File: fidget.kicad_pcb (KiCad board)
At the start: 2 copper layers, 80.5 x 73.5 mm, 88 parts, among them J1 KEYSTONE 120, J2 KEYSTONE 120, Q1 PEMZ7, U1 MCP73831-2ACI/MC, U2 ESP8285, U3 TLV70033DSE, U4 LIS2DE, U5 TPS60150, U6 TPS60150, U7 TPS60150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

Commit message: PCB design at 4am.. probably a bad idea
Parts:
- removed the C12 at (102.8, 128.8)
- removed the C13 at (104.8, 119.8)
- removed the C14 at (108.8, 126.0)
- removed TP3: RST, Measurement_Points:Measurement_Point_Round-SMD-Pad_Small
- removed the U5 at (113.2, 64.3)
- added C18: 2.2u, Capacitors_SMD:C_0603, F.Cu at (84.7, 71.8)
- added C19: 1u, Capacitors_SMD:C_0603, F.Cu at (85.6, 74.9)
- added C20: 2.2u, Capacitors_SMD:C_0603, F.Cu at (81.1, 72.3)
- added C23: 100n, Capacitors_SMD:C_0402, F.Cu at (86.8, 64.5)
- added U7: TPS60150, Housings_DFN_QFN:DFN-6-1EP_2x2mm_Pitch0.65mm, F.Cu at (83.4, 73.6)
- moved C17 72.2 mm to (107.5, 52.5), turned to 300 degrees
- moved U4 72.2 mm to (110.0, 102.5)
- moved U6 69.5 mm to (105.2, 53.8), turned to 210 degrees
- moved C16 69.3 mm to (103.0, 55.1), turned to 120 degrees
- moved C15 68.8 mm to (106.1, 55.8), turned to 210 degrees
- moved C10 60.8 mm to (100.0, 89.5)
- moved R9 55.4 mm to (112.7, 76.8), turned to 120 degrees
- moved R13 50.5 mm to (94.4, 85.6), turned to 180 degrees
- moved R8 50.4 mm to (111.5, 77.5), turned to 120 degrees
- moved R4 47.0 mm to (94.4, 86.8)
- moved C13 45.8 mm to (111.4, 80.0)
- moved U5 44.8 mm to (111.4, 82.6), turned to 90 degrees
- moved Q1 43.1 mm to (97.2, 86.2), turned to 180 degrees
- moved C12 42.9 mm to (109.2, 82.4), turned to 90 degrees
- moved C14 40.8 mm to (111.4, 85.2), turned to 180 degrees
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- renumbered C18 to C12, C19 to C13, C20 to C14, U7 to U5
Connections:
- C14 pad 1: +5P -> +5C
- U5 pad 3: +5P -> +5C
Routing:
- net +3V3: track 0.00 -> 55.1 mm, vias 0 -> 3
- net /IDX: track 0.00 -> 38.7 mm, vias 0 -> 2
- net +BATT: track 0.00 -> 37.1 mm
- net GND: track 0.00 -> 19.8 mm, vias 0 -> 52
- net +5C: track 0.00 -> 14.9 mm, vias 0 -> 2
- net +5F: track 0.00 -> 12.4 mm, vias 0 -> 2
- net /SCK: track 0.00 -> 9.42 mm, vias 0 -> 2
- net /LCK: track 0.00 -> 7.59 mm
- net /~CS~: track 0.00 -> 7.17 mm, vias 0 -> 2
- net Net-(D21-Pad2): track 0.00 -> 6.90 mm
- net Net-(D10-Pad2): track 0.00 -> 6.90 mm
- net /MOSI: track 0.00 -> 6.89 mm
- net /MISO: track 0.00 -> 6.86 mm, vias 0 -> 2
- net Net-(D21-Pad3): track 0.00 -> 5.97 mm
- net Net-(D10-Pad3): track 0.00 -> 5.97 mm
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- added copper zone on F.Cu, net +5C
- added copper zone on F.Cu, net +5F
- added copper zone on F.Cu, net +5P
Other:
- net class Default: clearance 0.2 -> 0.16
- rule pad_to_mask_clearance: 0.2 -> 0.1
- rule trace_clearance: 0.2 -> 0.16
- rule trace_min: 0.2 -> 0.16

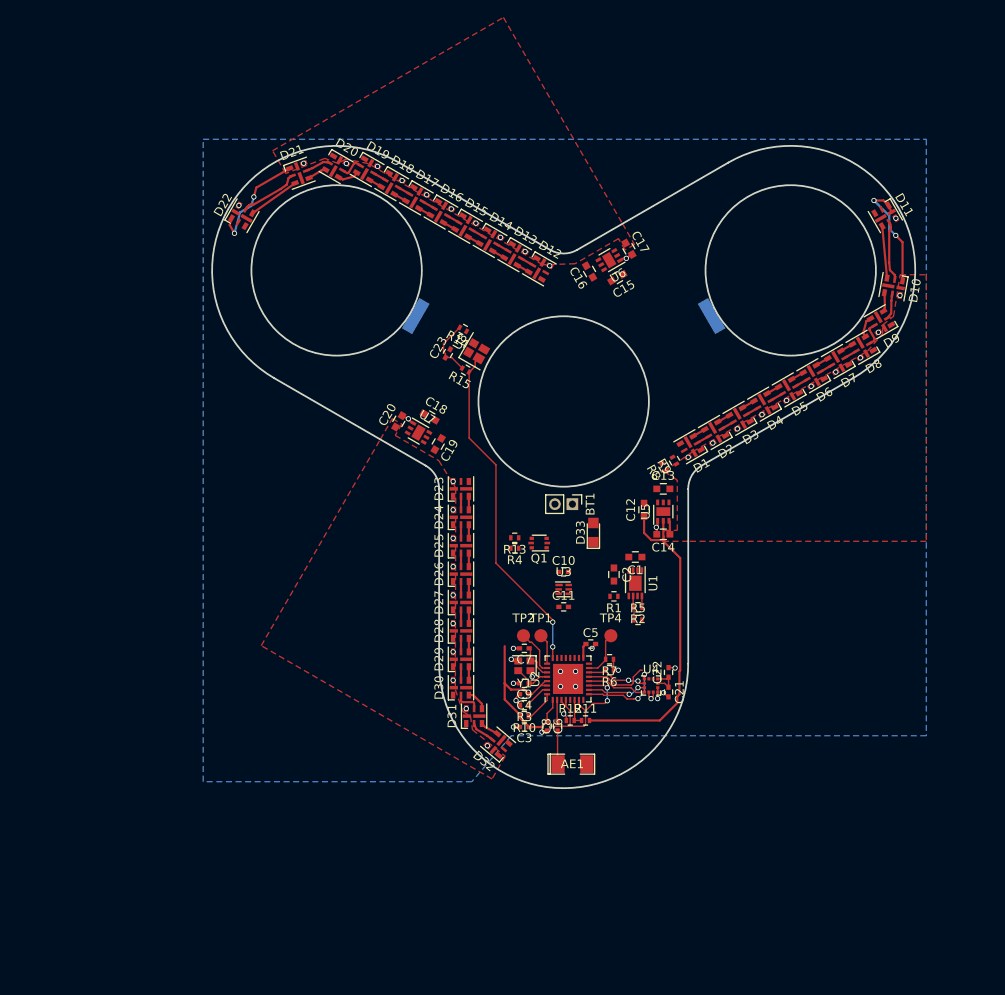
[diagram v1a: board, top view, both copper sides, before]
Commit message: RTFM: reverse polarity protection is already inside MCP73831
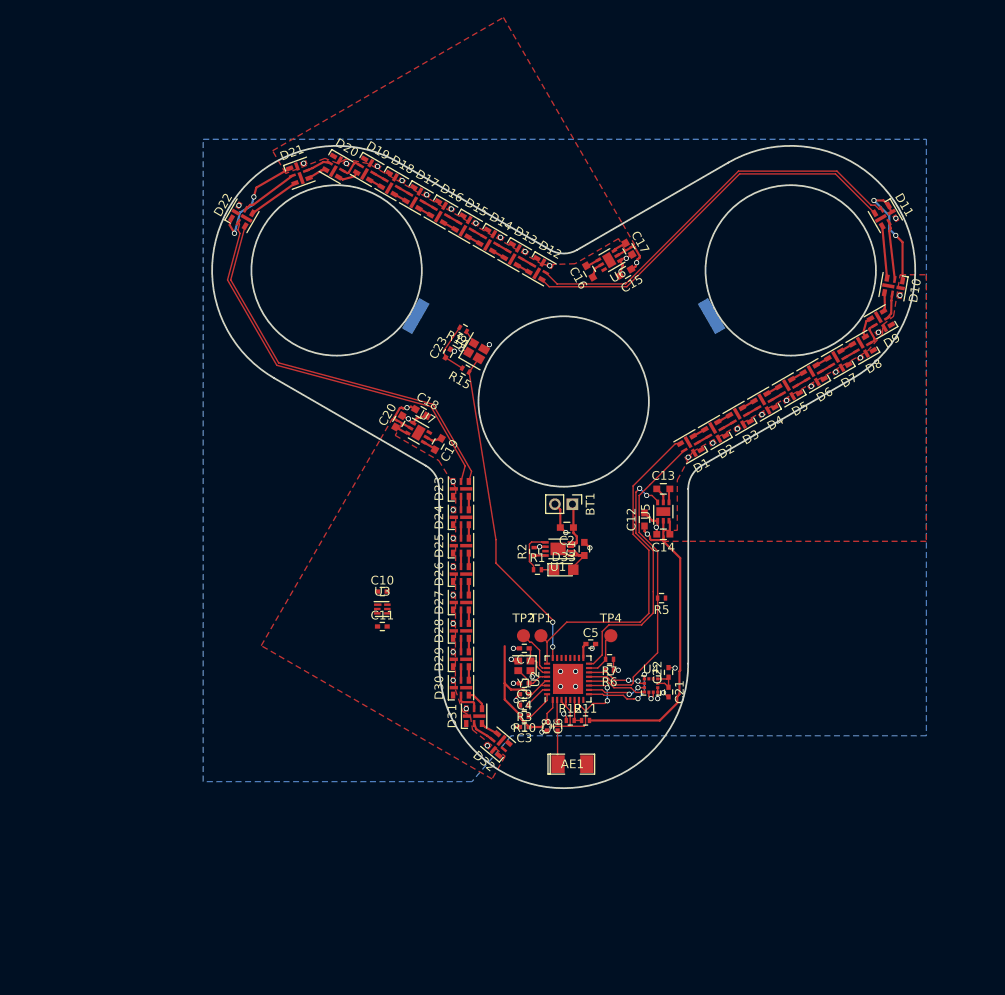
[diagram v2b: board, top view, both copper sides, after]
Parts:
- removed Q1: PEMZ7, TO_SOT_Packages_SMD:SOT-666
- removed R13, R4: 2k, Resistors_SMD:R_0402
- removed R8, R9: NC, Resistors_SMD:R_0402
- C6: value 12p -> 10p
- moved C10 20.9 mm to (79.2, 91.8)
- moved C11 20.9 mm to (79.2, 95.8)
- moved U3 20.9 mm to (79.2, 93.8)
- moved R2 13.5 mm to (96.6, 87.2), turned to 90 degrees
- moved U1 9.67 mm to (99.4, 86.9), turned to 180 degrees
- moved R1 9.27 mm to (97.0, 89.2), turned to 0 degrees
- moved C2 7.61 mm to (100.4, 84.4), turned to 180 degrees
- moved C1 5.91 mm to (102.4, 86.9), turned to 90 degrees
- moved D33 5.44 mm to (100.0, 89.2), turned to 0 degrees
- moved R5 3.68 mm to (111.2, 92.5), turned to 180 degrees
- moved C18 1.10 mm to (83.7, 71.3)
- moved C12 1.10 mm to (109.2, 83.5)
- moved C15 1.10 mm to (107.1, 55.2)
- renumbered J2 to J1, J1 to J2
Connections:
- J1 pad 1: GND -> +5V
- J2 pad 1: Net-(J1-Pad1) -> GND
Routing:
- net /LCK2: track 0.00 -> 46.1 mm
- net /LCK3: track 0.00 -> 46.1 mm
- net /LSO2: track 0.00 -> 45.7 mm
- net /LSO3: track 0.00 -> 45.7 mm
- net /LSO: track 3.49 -> 39.2 mm
- net /ENL: track 0.00 -> 29.4 mm, vias 0 -> 2
- net /LCK: track 7.59 -> 36.3 mm
- net +BATT: track 37.1 -> 53.1 mm, vias 0 -> 3
- net GND: track 19.8 -> 30.9 mm, vias 52 -> 58
- net +5V: track 0.00 -> 5.46 mm
- net Net-(R1-Pad1): track 0.00 -> 5.07 mm
- net Net-(C13-Pad1): track 0.00 -> 1.86 mm
- net Net-(C19-Pad1): track 0.00 -> 1.86 mm
- net Net-(C16-Pad1): track 0.00 -> 1.86 mm
- net Net-(R14-Pad1): track 0.00 -> 1.60 mm
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
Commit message: routing done
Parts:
- added TP3: GND, Measurement_Points:Measurement_Point_Round-SMD-Pad_Small, F.Cu at (101.4, 96.8)
- moved C10 14.8 mm to (93.8, 89.0)
- moved C11 14.8 mm to (93.8, 93.0)
- moved U3 14.8 mm to (93.8, 91.0)
- moved C5 0.51 mm to (103.0, 98.2)
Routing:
- net GND: track 30.9 -> 325.8 mm, vias 58 -> 183
- net +BATT: track 53.1 -> 136.6 mm, vias 3 -> 6
- net +3V3: track 54.7 -> 132.9 mm, vias 3 -> 9
- net /ENL: track 29.4 -> 86.1 mm, vias 2 -> 7
- net +5V: track 5.46 -> 41.2 mm, vias 0 -> 1
- net /IDX: track 37.6 -> 40.3 mm, vias 2 -> 4
- net +5F: track 14.0 -> 14.9 mm
- added copper zone on F.Cu, net GND
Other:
- net class Default: clearance 0.16 -> 0.15
- rule trace_clearance: 0.16 -> 0.15

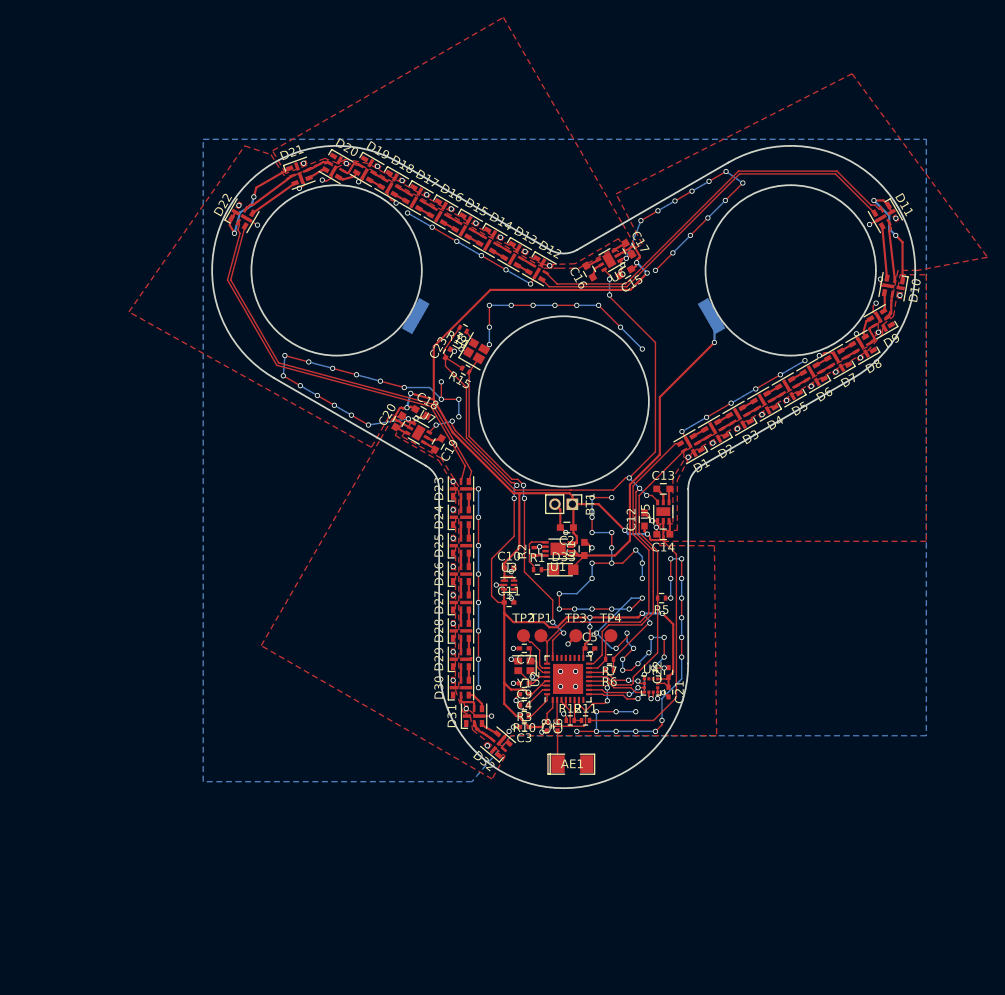
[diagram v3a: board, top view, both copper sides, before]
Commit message: cleaned up silkscreen
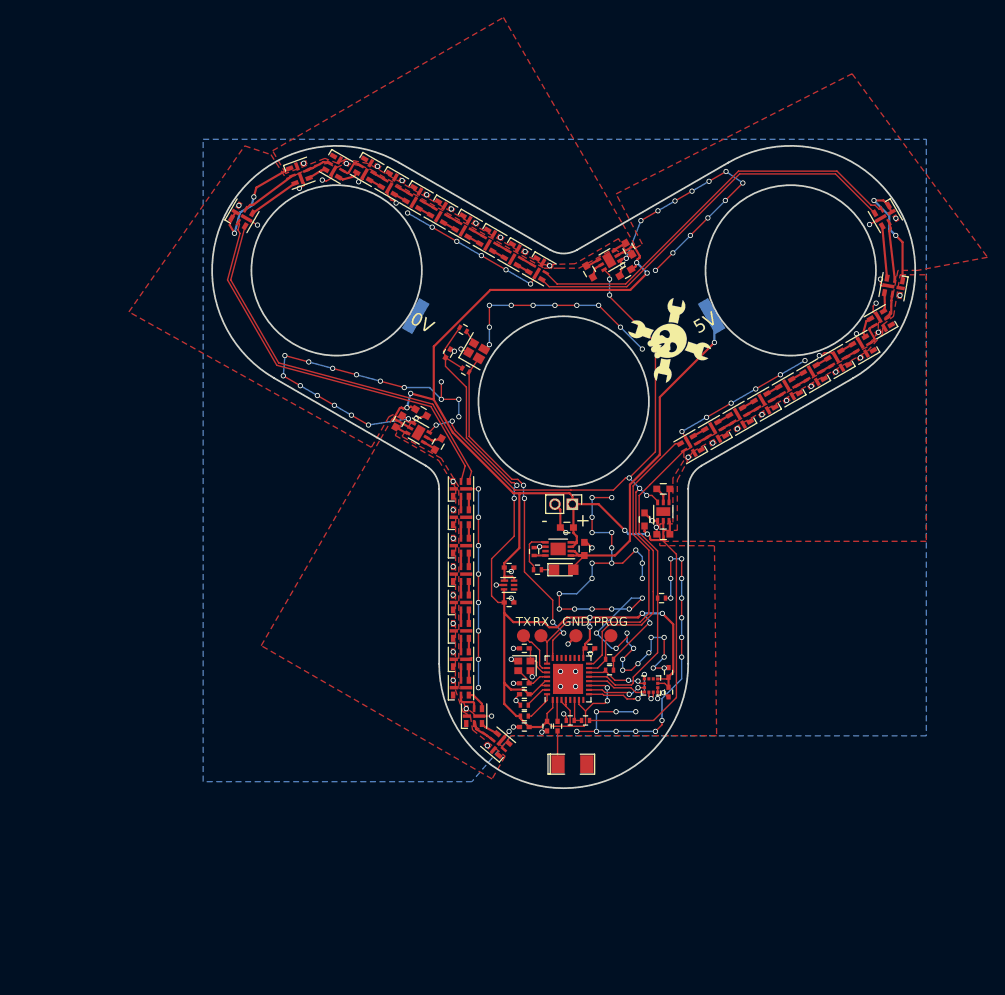
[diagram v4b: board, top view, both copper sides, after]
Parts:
- added G1: HACKADAY, parts:wrencher_8mm, F.Cu at (112.1, 63.0)
- added G2: OPEN_HARDWARE, Symbols:OSHW-Logo_7.5x8mm_SilkScreen, B.Cu at (93.0, 85.2)
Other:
- board text added: "+"
- board text added: "-"
- board text added: "0V"
- board text added: "5V"

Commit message: added level shifter
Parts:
- removed R5: 12k, Resistors_SMD:R_0402
- added U9: NTS0102GT, parts:SOT833-1, F.Cu at (110.2, 93.5)
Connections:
- D1 pad 4: /LSO -> /LSO1
- D1 pad 5: /LCK -> /LCK1
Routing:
- net /LSO: track 39.2 -> 16.7 mm
- net /LCK: track 36.3 -> 14.6 mm
- net /LSO1: track 0.00 -> 21.1 mm
- net /LCK1: track 0.00 -> 20.5 mm
- net +5C: track 14.9 -> 24.3 mm, vias 2 -> 4
- net /ENL: track 86.1 -> 89.6 mm, vias 7 -> 8
- net +5V: track 41.2 -> 42.1 mm
- net GND: track 325.8 -> 326.4 mm, vias 183 -> 181
- net +3V3: track 132.9 -> 132.7 mm, vias 9 -> 8

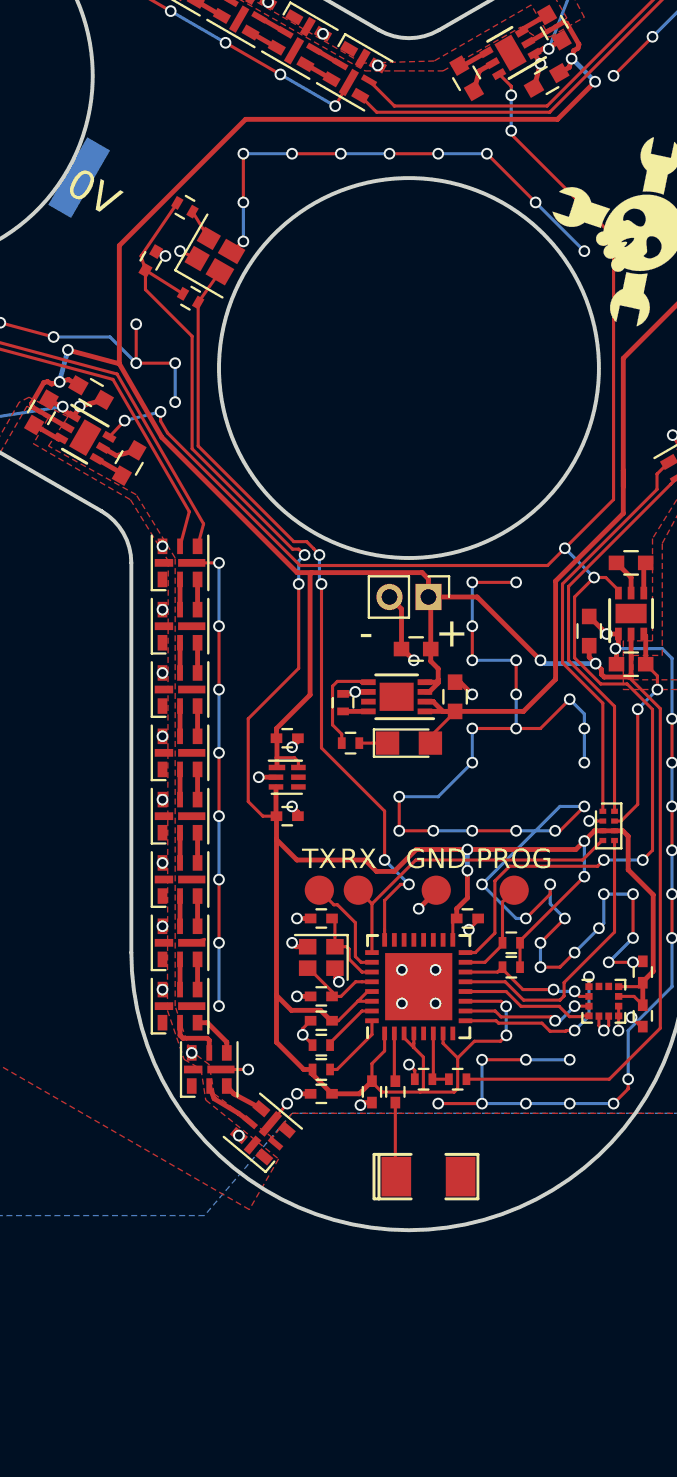
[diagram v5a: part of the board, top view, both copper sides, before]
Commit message: switched to hall sensor
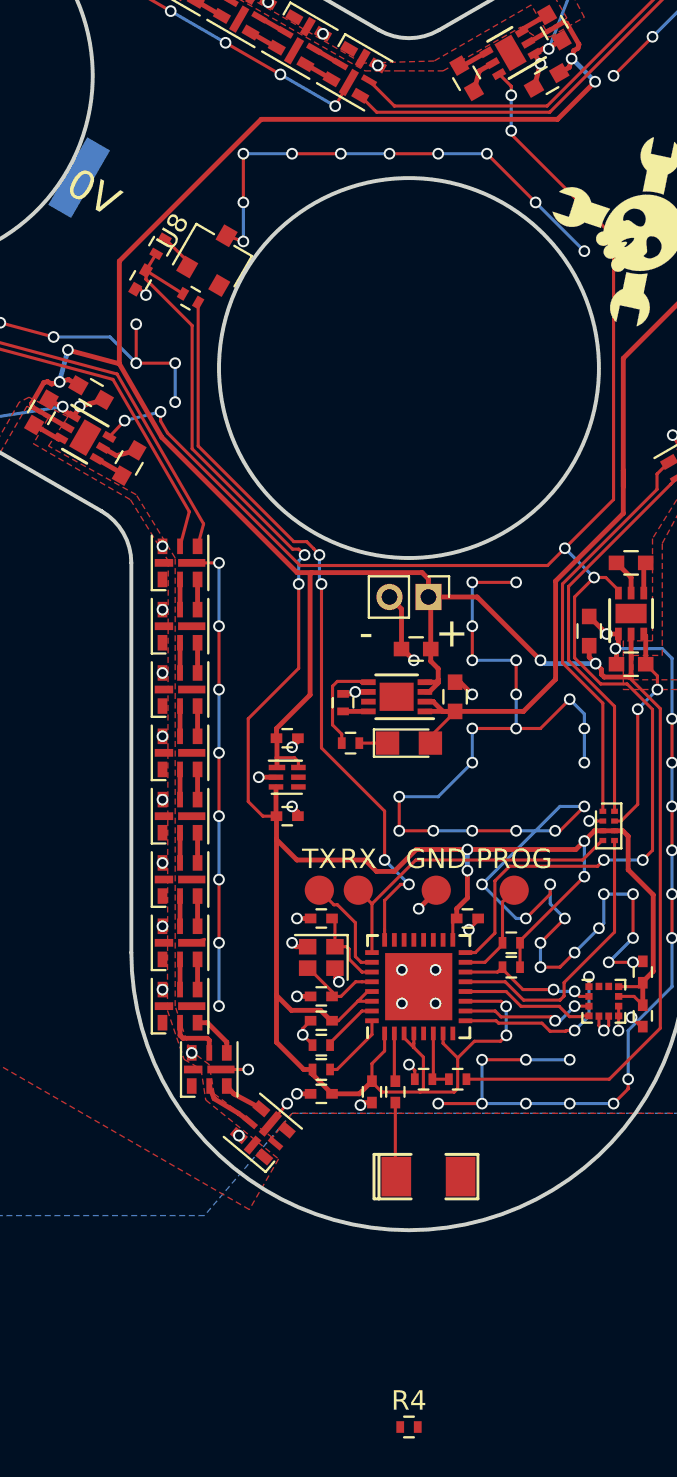
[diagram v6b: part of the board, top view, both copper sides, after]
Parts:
- added R4: 2k, Resistors_SMD:R_0402, F.Cu at (100.0, 124.4)
- U8: value VCNT2020 -> TLV4946-2K; footprint parts:VCNT2020 -> TO_SOT_Packages_SMD:SC-59
- moved R14 2.36 mm to (87.2, 63.8), turned to 240 degrees
- moved C23 1.11 mm to (86.2, 65.5), turned to 240 degrees
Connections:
- U8 pad 1: GND -> Net-(R14-Pad1)
- U8 pad 3: Net-(R14-Pad1) -> GND
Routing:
- net +3V3: track 132.7 -> 129.6 mm
- net /IDX: track 40.3 -> 38.3 mm
- net GND: track 326.4 -> 325.7 mm, vias 181 -> 180
